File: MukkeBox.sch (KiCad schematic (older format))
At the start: 52 parts, among them J101 ST_Link_V2_10P, J104 Conn_02x05_Odd_Even, J107 PinHeader, J108 PinHeader, J109 PinHeader, Q101 NTK3043N, U101 TPS7B82-Q1, U102 STM32F030C6Tx_MukkeBox, Y101 FOXSDLF/080-20

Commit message: Board abgeschickt
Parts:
- added C114: 100nF, Capacitor_SMD:C_0603_1608Metric_Pad1.05x0.95mm_HandSolder, symbol Device:C_Small
- added D101: LED_Small, LED_THT:LED_D3.0mm, symbol Device:LED_Small
- added R104: 1M, Resistor_SMD:R_0603_1608Metric_Pad1.05x0.95mm_HandSolder, symbol Device:R_Small
- added R124: 1K, Resistor_SMD:R_0603_1608Metric_Pad1.05x0.95mm_HandSolder, symbol Device:R_Small
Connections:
- net GND: now also C114.2, D101.1 (K), R104.1
- net POWER_OFF_O: now also R104.2
- net at Q101.1 (G), R114.2: now also C114.1
- net at U102.42 (PB6/AKKU_100): now also R124.1
- new net: D101.2 (A), R124.2
- no-connect marks 5 -> 4
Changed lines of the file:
@@
 $EndComp
 Wire Wire Line
-	3150 4250 3150 4500
+	3150 4250 3150 4450
 Text Label 4350 5150 0    50   ~ 0
 POWER_OFF_O
@@
 	3400 5400 4250 5400
 Wire Wire Line
-	5450 5150 3750 5150
-Wire Wire Line
-	3750 5150 3750 4050
+	5450 5150 3900 5150
+Wire Wire Line
+	3900 5150 3900 4050
 Wire Wire Line
 	8100 4900 7450 4900
@@
 F 1 "NTK3043N" H 3456 4005 50  0000 L CNN
 F 2 "Package_TO_SOT_SMD:SOT-723" H 3450 4150 50  0001 C CNN
-F 3 "~" H 3250 4050 50  0001 C CNN
+F 3 "https://www.mouser.de/datasheet/2/308/NTK3043N-D-1814099.pdf" H 3250 4050 50  0001 C CNN
 	1    3250 4050
 	-1   0    0    -1
 $EndComp
 Wire Wire Line
-	3650 4050 3750 4050
+	3650 4050 3700 4050
 Text GLabel 4750 6000 0    50   Input ~ 0
 PACK_VOLTAGE
@@
 	9850 3900 9850 4200
 Connection ~ 9850 4200
-Wire Wire Line
-	9700 3650 9700 3800
-Connection ~ 9700 3800
-Wire Wire Line
-	10550 3650 10550 3800
-Connection ~ 10550 3800
 $Comp
 L power:GND #PWR0184
@@
 Wire Wire Line
 	7950 5900 7450 5900
-NoConn ~ 7450 6000
 $Comp
 L Connector_Generic:Conn_02x03_Counter_Clockwise J109
@@
 Wire Wire Line
 	10150 1200 10150 1400
+$Comp
+L Device:R_Small R104
+U 1 1 5E9BF0D7
+P 3700 4350
+F 0 "R104" H 3550 4300 50  0000 C CNN
+F 1 "1M" H 3600 4400 50  0000 C CNN
+F 2 "Resistor_SMD:R_0603_1608Metric_Pad1.05x0.95mm_HandSolder" H 3700 4350 50  0001 C CNN
+F 3 "~" H 3700 4350 50  0001 C CNN
+	1    3700 4350
+	-1   0    0    1
+$EndComp
+$Comp
+L Device:C_Small C114
+U 1 1 5E9BF274
+P 3450 4350
+F 0 "C114" H 3150 4400 50  0000 L CNN
+F 1 "100nF" H 3150 4300 50  0000 L CNN
+F 2 "Capacitor_SMD:C_0603_1608Metric_Pad1.05x0.95mm_HandSolder" H 3450 4350 50  0001 C CNN
+F 3 "~" H 3450 4350 50  0001 C CNN
+	1    3450 4350
+	1    0    0    -1
+$EndComp
+Wire Wire Line
+	3700 4250 3700 4050
+Connection ~ 3700 4050
+Wire Wire Line
+	3700 4050 3900 4050
+Wire Wire Line
+	3450 4250 3450 4050
+Connection ~ 3450 4050
+Wire Wire Line
+	3700 4450 3450 4450
+Wire Wire Line
+	3150 4450 3450 4450
+Connection ~ 3150 4450
+Wire Wire Line
+	3150 4450 3150 4500
+Connection ~ 3450 4450
+$Comp
+L Device:R_Small R124
+U 1 1 5EA46EE7
+P 7850 6250
+F 0 "R124" V 7650 6250 50  0000 C CNN
+F 1 "1K" V 7750 6250 50  0000 C CNN
+F 2 "Resistor_SMD:R_0603_1608Metric_Pad1.05x0.95mm_HandSolder" H 7850 6250 50  0001 C CNN
+F 3 "~" H 7850 6250 50  0001 C CNN
+	1    7850 6250
+	0    -1   -1   0
+$EndComp
+$Comp
+L Device:LED_Small D101
+U 1 1 5EA471AF
+P 8200 6250
+F 0 "D101" H 8200 6045 50  0000 C CNN
+F 1 "LED_Small" H 8200 6136 50  0000 C CNN
+F 2 "LED_THT:LED_D3.0mm" V 8200 6250 50  0001 C CNN
+F 3 "~" V 8200 6250 50  0001 C CNN
+	1    8200 6250
+	-1   0    0    1
+$EndComp
+$Comp
+L power:GND #PWR0193
+U 1 1 5EA47367
+P 8500 6250
+F 0 "#PWR0193" H 8500 6000 50  0001 C CNN
+F 1 "GND" H 8505 6077 50  0000 C CNN
+F 2 "" H 8500 6250 50  0001 C CNN
+F 3 "" H 8500 6250 50  0001 C CNN
+	1    8500 6250
+	1    0    0    -1
+$EndComp
+Wire Wire Line
+	8500 6250 8300 6250
+Wire Wire Line
+	8100 6250 7950 6250
+Wire Wire Line
+	7550 6250 7550 6000
+Wire Wire Line
+	7550 6000 7450 6000
+Wire Wire Line
+	7550 6250 7750 6250
 $EndSCHEMATC

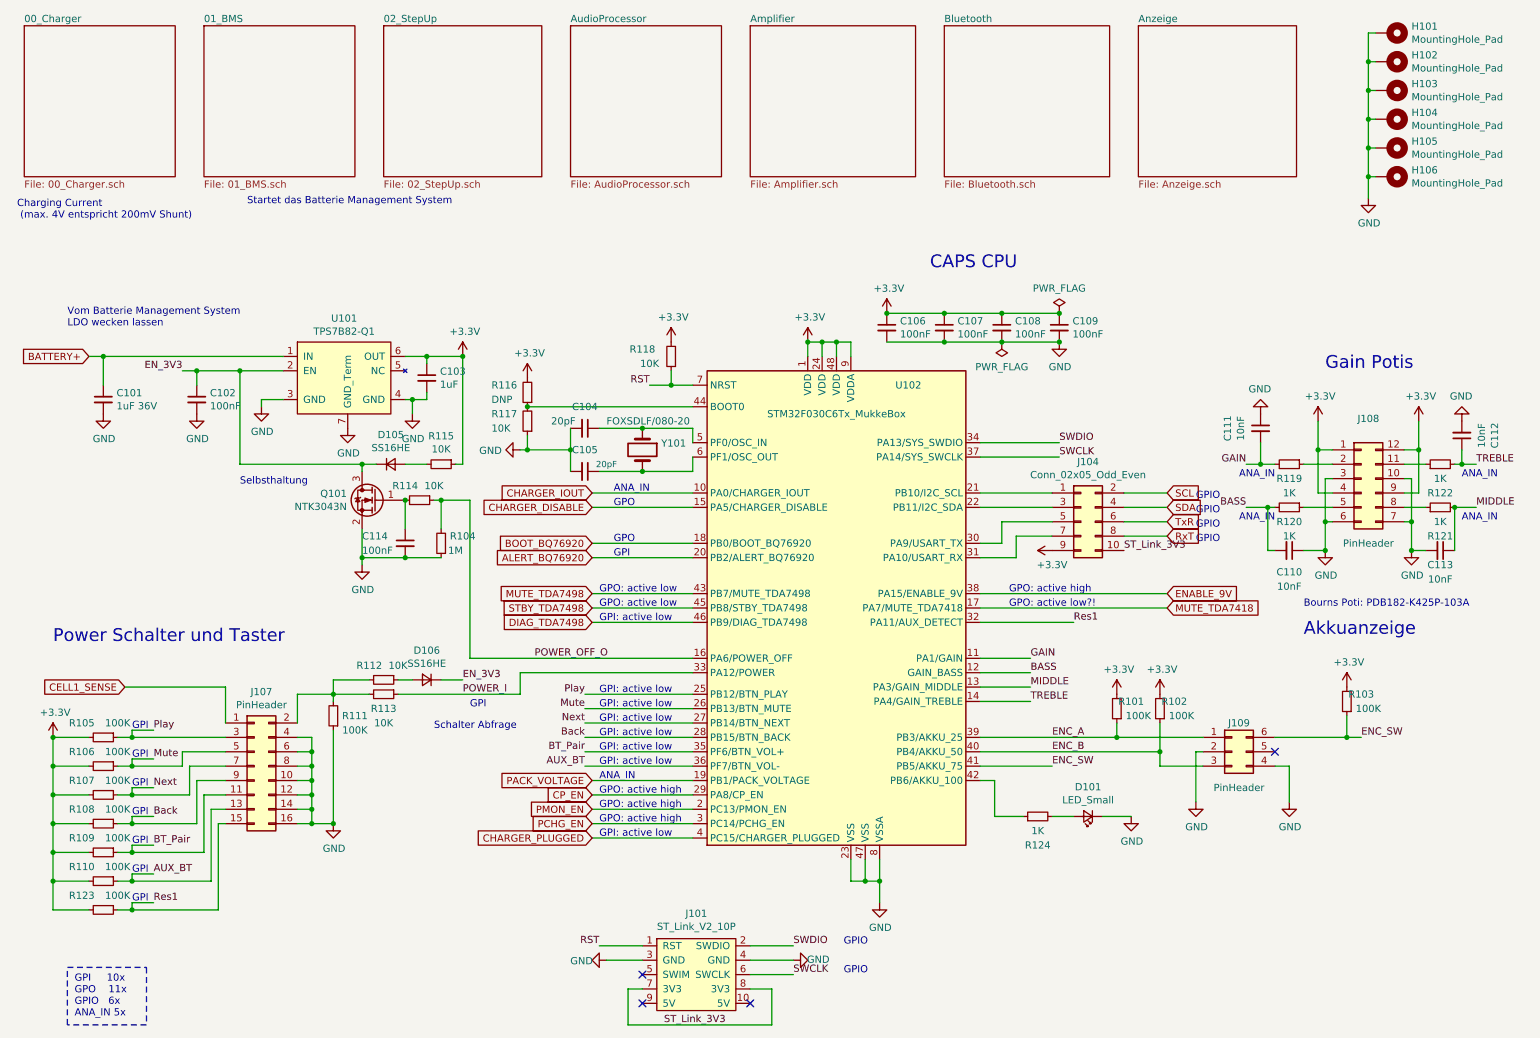
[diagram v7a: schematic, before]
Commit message: mute and stdby tda7498 geändert, tda7418 durch tda7719 ersetzt, xs3868 durch bk8000l ersetzt, 3v3 stepdown statt LDO. BMS gelöscht.  TODO: Möglichkeit stepup und stepdown als modul aufzusetzen
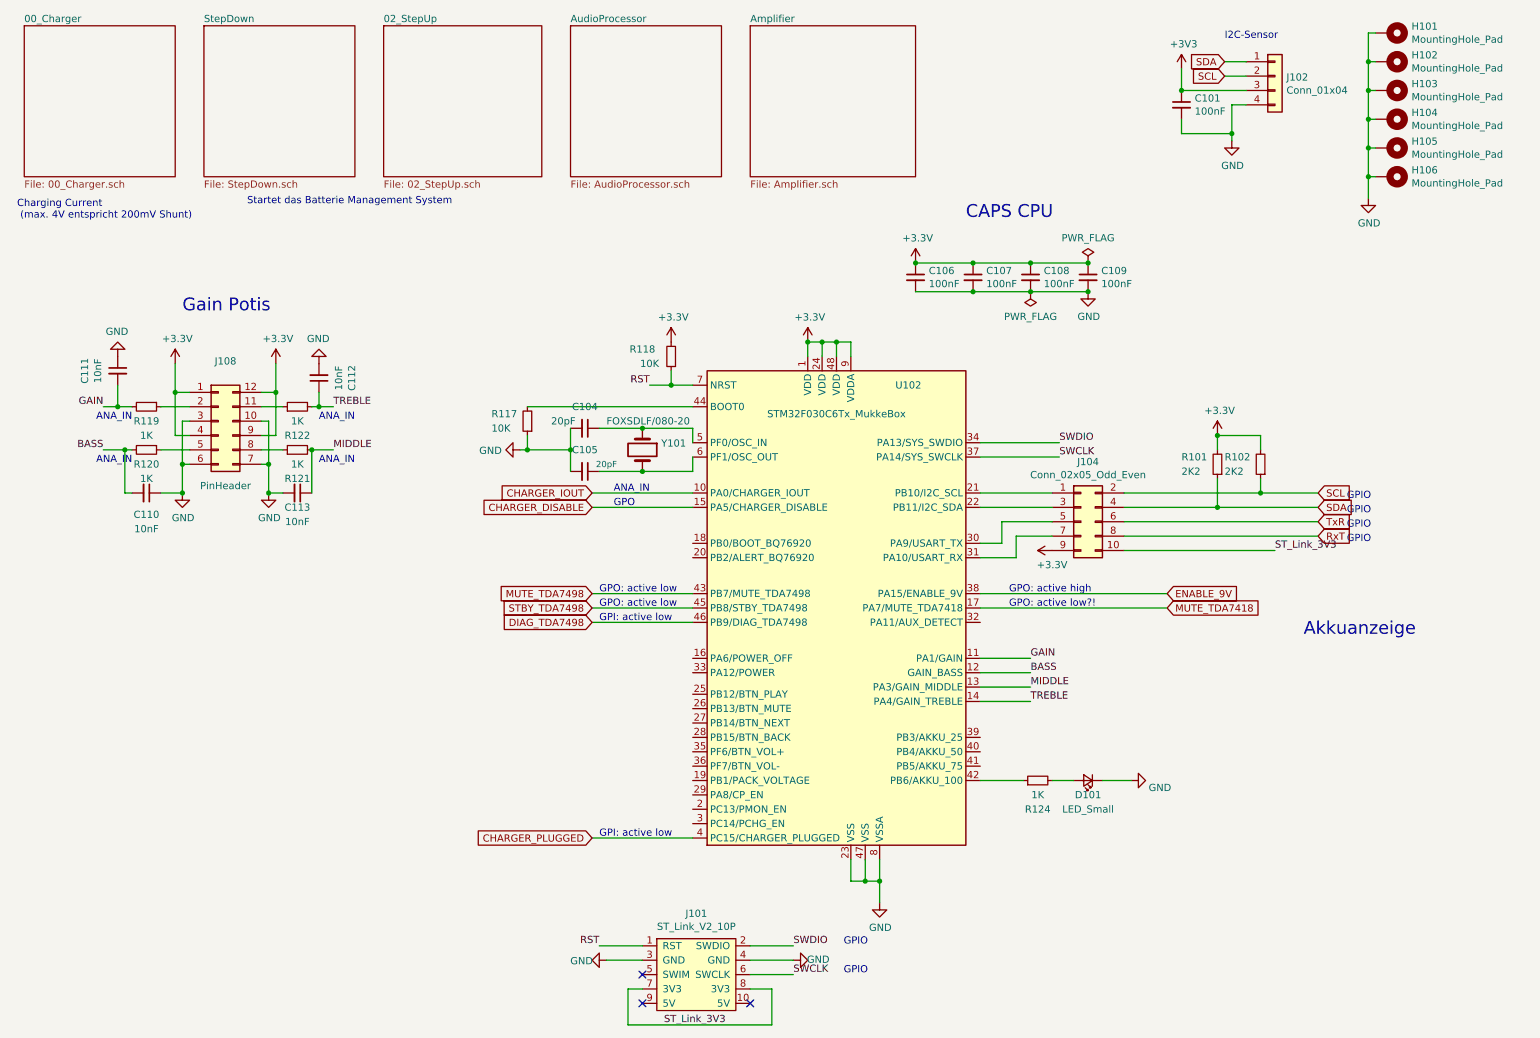
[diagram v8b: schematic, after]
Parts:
- removed C102, C114: 100nF, Capacitor_SMD:C_0603_1608Metric_Pad1.05x0.95mm_HandSolder, symbol Device:C_Small
- removed C103: 1uF, Capacitor_SMD:C_0603_1608Metric_Pad1.05x0.95mm_HandSolder, symbol Device:C_Small
- removed D105, D106: SS16HE, Diode_SMD:D_SOD-323, symbol Device:D_Small
- removed J107: PinHeader, Connector_PinHeader_2.54mm:PinHeader_2x08_P2.54mm_Vertical_SMD, symbol Connector_Generic:Conn_02x08_Odd_Even
- removed J109: PinHeader, Connector_PinHeader_2.54mm:PinHeader_2x03_P2.54mm_Vertical_SMD, symbol Connector_Generic:Conn_02x03_Counter_Clockwise
- removed Q101: NTK3043N, Package_TO_SOT_SMD:SOT-723, symbol Device:Q_NMOS_GSD
- removed R103, R105, R106, R107, R108, R109, R110, R111, R123: 100K, Resistor_SMD:R_0603_1608Metric_Pad1.05x0.95mm_HandSolder, symbol Device:R_Small
- removed R104: 1M, Resistor_SMD:R_0603_1608Metric_Pad1.05x0.95mm_HandSolder, symbol Device:R_Small
- removed R112, R113, R114, R115: 10K, Resistor_SMD:R_0603_1608Metric_Pad1.05x0.95mm_HandSolder, symbol Device:R_Small
- removed R116: DNP, Resistor_SMD:R_0603_1608Metric_Pad1.05x0.95mm_HandSolder, symbol Device:R_Small
- removed U101: TPS7B82-Q1, Package_DFN_QFN:Texas_S-PWSON-N6_ThermalVias, symbol Regulator_Linear:TPS7B82-Q1
- added J102: Conn_01x04, Connector_PinHeader_2.54mm:PinHeader_1x04_P2.54mm_Vertical, symbol Connector_Generic:Conn_01x04
- C101: value 1uF 36V -> 100nF
- J104: footprint Connector_PinHeader_2.54mm:PinHeader_2x05_P2.54mm_Vertical_SMD -> Connector_PinHeader_2.54mm:PinHeader_2x05_P2.54mm_Vertical
- R101, R102: value 100K -> 2K2
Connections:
- net BATTERY+ is gone; now on net +3V3: C101.1
- net +3V3: now also J102.3 (Pin_3)
- net GND: now also J102.4 (Pin_4)
- net SCL: now also R102.1, J102.2 (Pin_2)
- net SDA: now also R101.1, J102.1 (Pin_1)
- net ALERT_BQ76920: no longer names the net of U102.20 (PB2/ALERT_BQ76920)
- net AUX_BT: no longer names the net of U102.36 (PF7/BTN_VOL-)
- net BOOT_BQ76920: no longer names the net of U102.18 (PB0/BOOT_BQ76920)
- net BT_Pair: no longer names the net of U102.35 (PF6/BTN_VOL+)
- net Back: no longer names the net of U102.28 (PB15/BTN_BACK)
- net CP_EN: no longer names the net of U102.29 (PA8/CP_EN)
- net ENC_A: no longer names the net of U102.39 (PB3/AKKU_25)
- net ENC_A: no longer R101.1
- net ENC_B: no longer names the net of U102.40 (PB4/AKKU_50)
- net ENC_B: no longer R102.1
- net ENC_SW: no longer names the net of U102.41 (PB5/AKKU_75)
- net Mute: no longer names the net of U102.26 (PB13/BTN_MUTE)
- net Next: no longer names the net of U102.27 (PB14/BTN_NEXT)
- net PACK_VOLTAGE: no longer names the net of U102.19 (PB1/PACK_VOLTAGE)
- net PCHG_EN: no longer names the net of U102.3 (PC14/PCHG_EN)
- net PMON_EN: no longer names the net of U102.2 (PC13/PMON_EN)
- net POWER_I: no longer names the net of U102.33 (PA12/POWER)
- net POWER_OFF_O: no longer names the net of U102.16 (PA6/POWER_OFF)
- net Play: no longer names the net of U102.25 (PB12/BTN_PLAY)
- net Res1: no longer names the net of U102.32 (PA11/AUX_DETECT)
- no-connect marks 4 -> 3
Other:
- note added: "I2C-Sensor"
- note removed: "Bourns Poti: PDB182-K425P-103A"
- note removed: "GPI"
- note removed: "GPI 10x\nGPO 11x\nGPIO 6x\nANA_IN 5x"
- note removed: "Power Schalter und Taster"
- note removed: "Schalter Abfrage"
- note removed: "Selbsthaltung"
- note removed: "Vom Batterie Management System\nLDO wecken lassen"
- moved on the sheet: C106, C107, C108, C109, C110, C111, C112, C113, D101, J108, R119, R120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
